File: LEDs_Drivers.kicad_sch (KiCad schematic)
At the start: 9 parts, among them J4 LEDs Controller Connector, U1 A009 BuckBlock or LDDS-HWB, U2 A009 BuckBlock or LDDS-HWB, U3 A009 BuckBlock or LDDS-HWB, U6 A009 BuckBlock or LDDS-HWB

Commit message: Using two LM317s instead of a LM7812 + LM7805 and KiCAD 8.0.3rc1
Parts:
- renumbered D2 to D5, D1 to D6, D3 to D7, D4 to D8, U6 to U13, U1 to U14, U2 to U15, U3 to U16

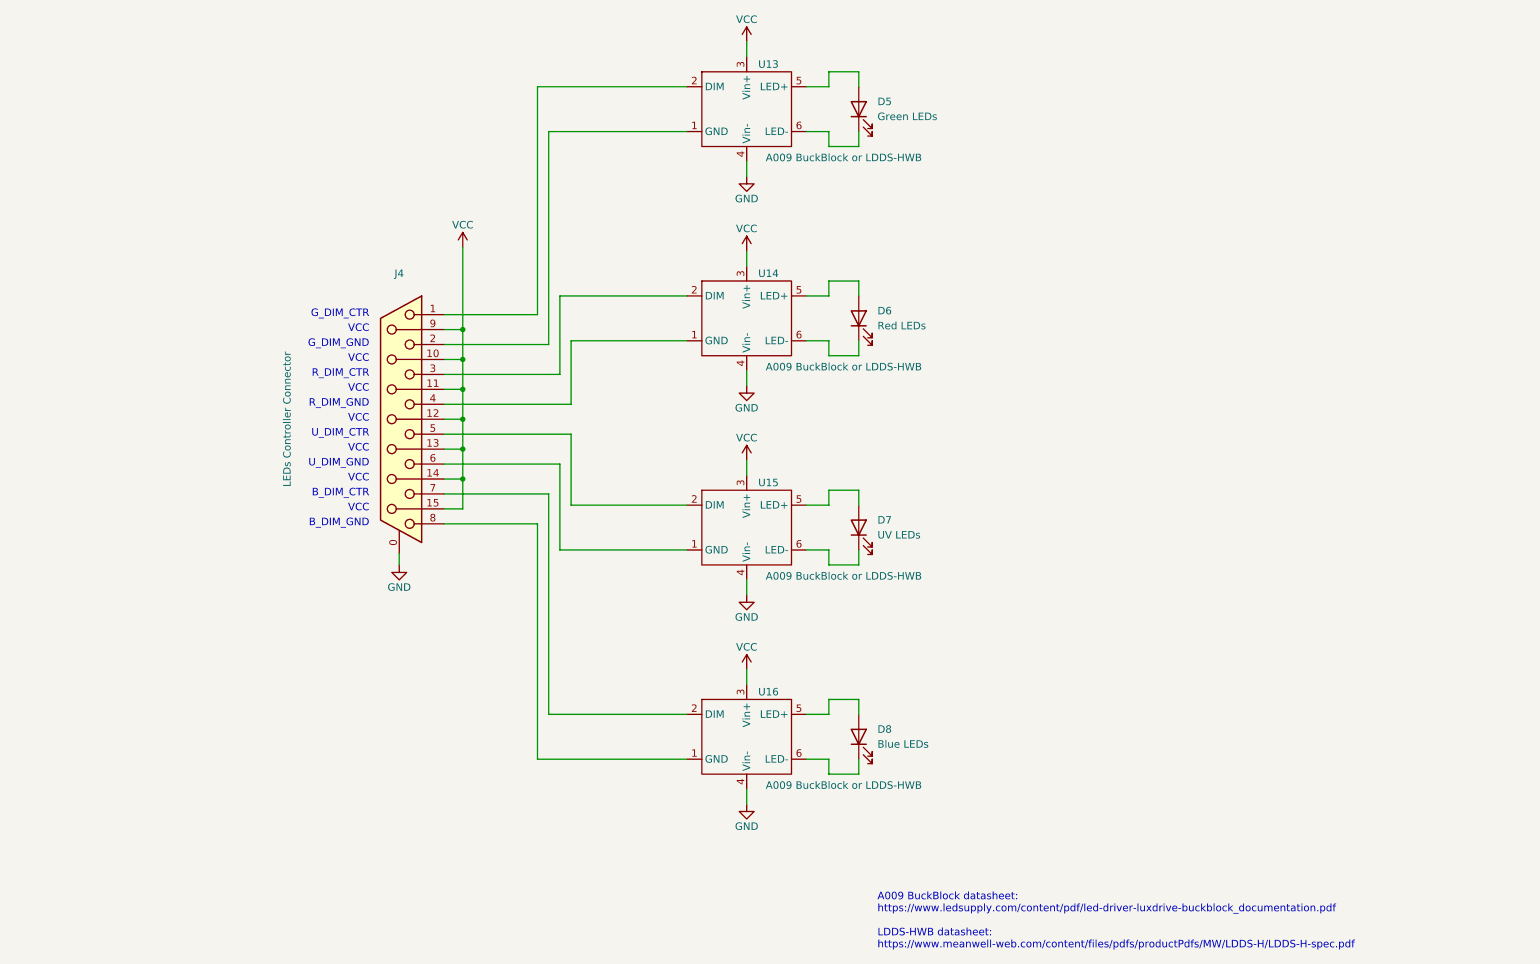
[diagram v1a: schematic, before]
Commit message: - Power rack alternatives: either two LM317s or LM7812 + LM7805 - Added channels SPDT selectors for foot switch or external output enable control
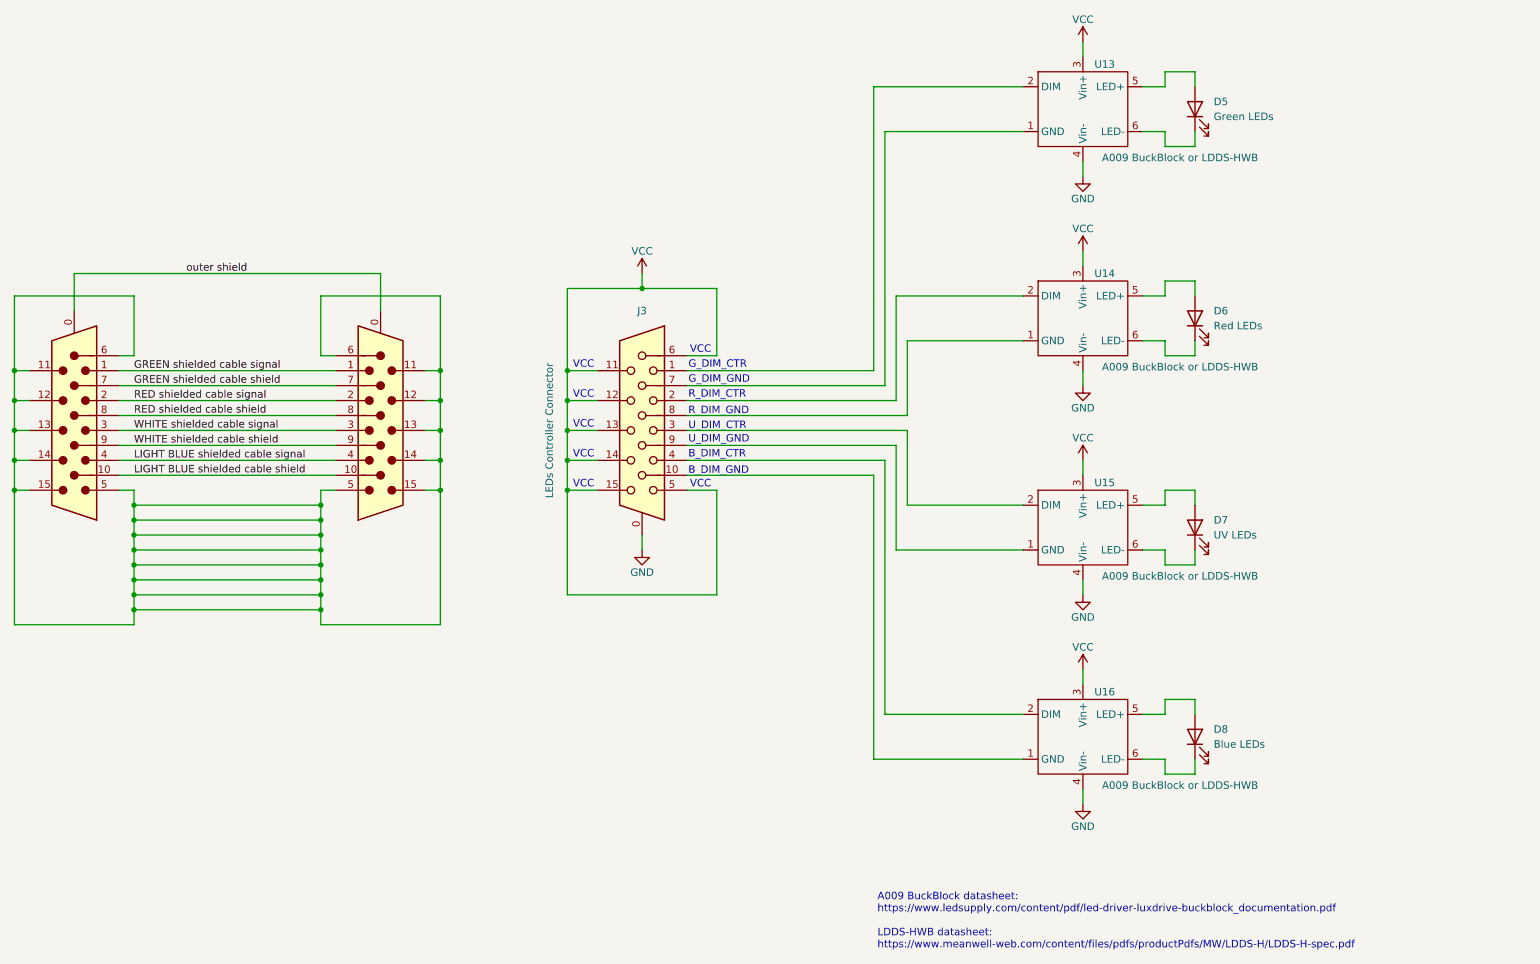
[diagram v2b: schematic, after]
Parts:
- removed J4: LEDs Controller Connector, symbol Connector:DB15_Female_MountingHoles
- added J3: LEDs Controller Connector, symbol Connector:DE15_Receptacle_HighDensity_MountingHoles
- added J4, J6: DE15_Plug_HighDensity_MountingHoles, symbol Connector:DE15_Plug_HighDensity_MountingHoles
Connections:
- net GND: now also J3.0
- net VCC: now also J3.11, J3.12, J3.13, J3.14, J3.15, J3.5, J3.6
- net at U13.2 (DIM): now also J3.1
- net at U13.1 (GND): now also J3.7
- net at U14.2 (DIM): now also J3.2
- net at U14.1 (GND): now also J3.8
- net at U15.2 (DIM): now also J3.3
- net at U15.1 (GND): now also J3.9
- net at U16.2 (DIM): now also J3.4
- net at U16.1 (GND): now also J3.10
- new net: J4.11, J4.12, J4.13, J4.14, J4.15, J4.5, J4.6, J6.11, J6.12, J6.13, J6.14, J6.15, J6.5, J6.6
- new net GREEN shielded cable shield: J4.7, J6.7
- new net GREEN shielded cable signal: J4.1, J6.1
- new net LIGHT BLUE shielded cable shield: J4.10, J6.10
- new net LIGHT BLUE shielded cable signal: J4.4, J6.4
- new net RED shielded cable shield: J4.8, J6.8
- new net RED shielded cable signal: J4.2, J6.2
- new net WHITE shielded cable shield: J4.9, J6.9
- new net WHITE shielded cable signal: J4.3, J6.3
- new net outer shield: J4.0, J6.0
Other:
- moved on the sheet: D5, D6, D7, D8, U13, U14, U15, U16

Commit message: Adding capacitors to stabilize voltages, changed the LED driver connector
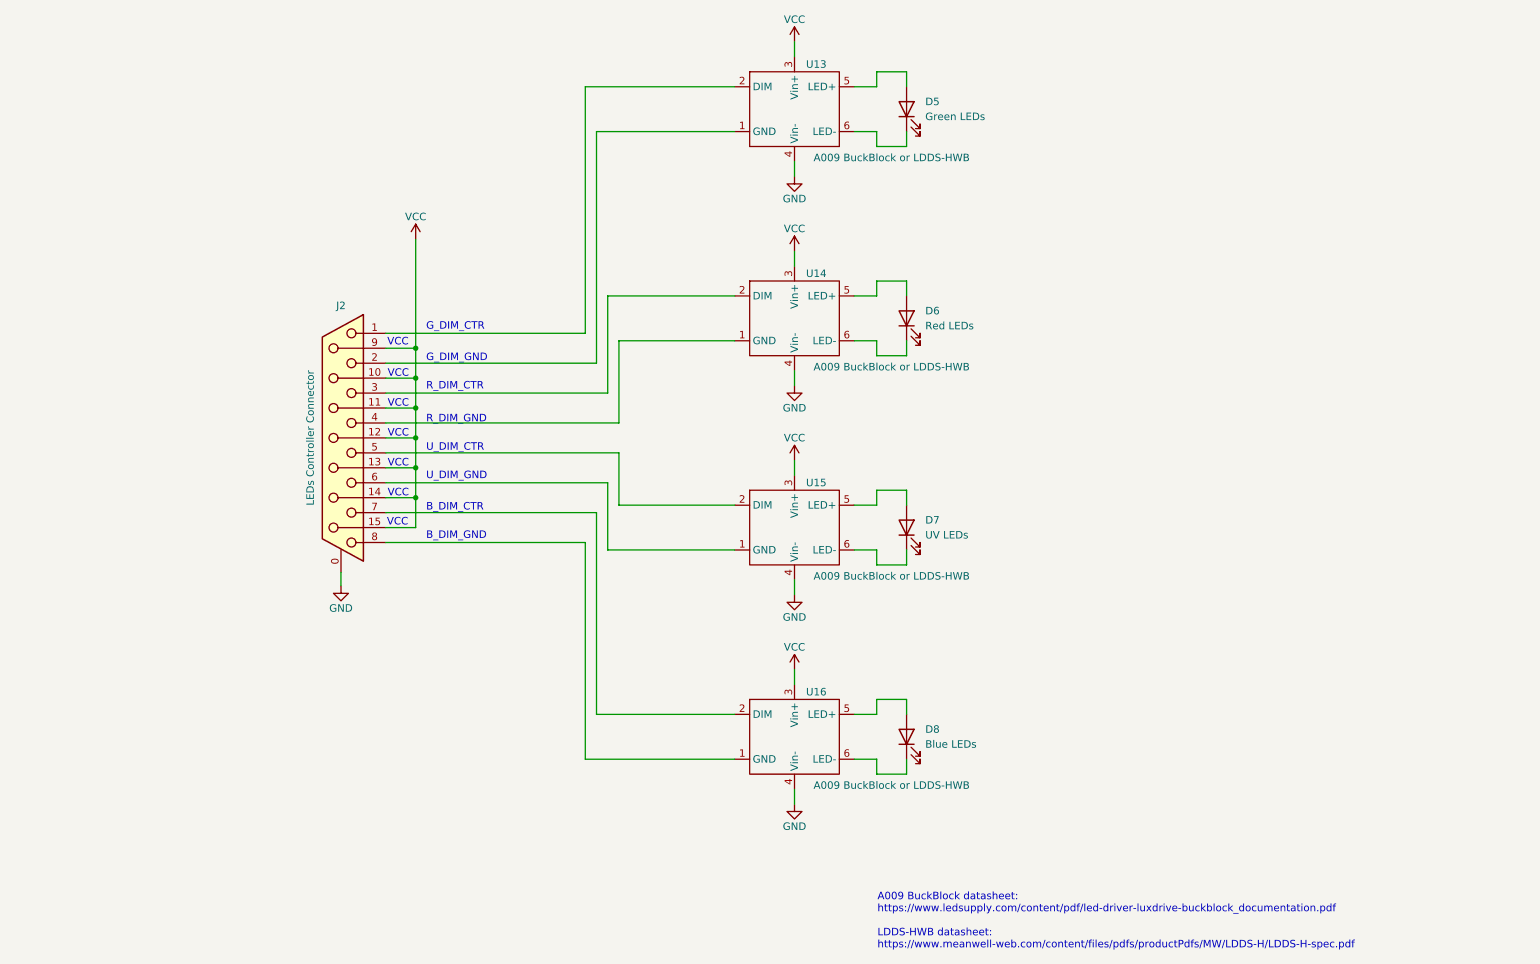
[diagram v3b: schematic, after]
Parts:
- removed J3: LEDs Controller Connector, symbol Connector:DE15_Receptacle_HighDensity_MountingHoles
- removed J4, J6: DE15_Plug_HighDensity_MountingHoles, symbol Connector:DE15_Plug_HighDensity_MountingHoles
- added J2: LEDs Controller Connector, symbol Connector:DA15_Receptacle_MountingHoles
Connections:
- net GND: now also J2.0 (PAD)
- net VCC: now also J2.10 (P10), J2.11 (P111), J2.12 (P12), J2.13 (P13), J2.14 (P14), J2.15 (P15), J2.9 (P9)
- net at U14.1 (GND): now also J2.4
- net at U14.2 (DIM): now also J2.3
- net at U13.2 (DIM): now also J2.1
- net at U16.1 (GND): now also J2.8
- net at U15.2 (DIM): now also J2.5
- net at U16.2 (DIM): now also J2.7
- net at U13.1 (GND): now also J2.2
- net at U15.1 (GND): now also J2.6
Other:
- moved on the sheet: D5, D6, D7, D8, U13, U14, U15, U16
